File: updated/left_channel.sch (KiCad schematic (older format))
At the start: 24 parts, among them J2 Left 8 ohms, J3 Left 0 ohms, J7 Conn_Coaxial, T1 AudioTxfmr

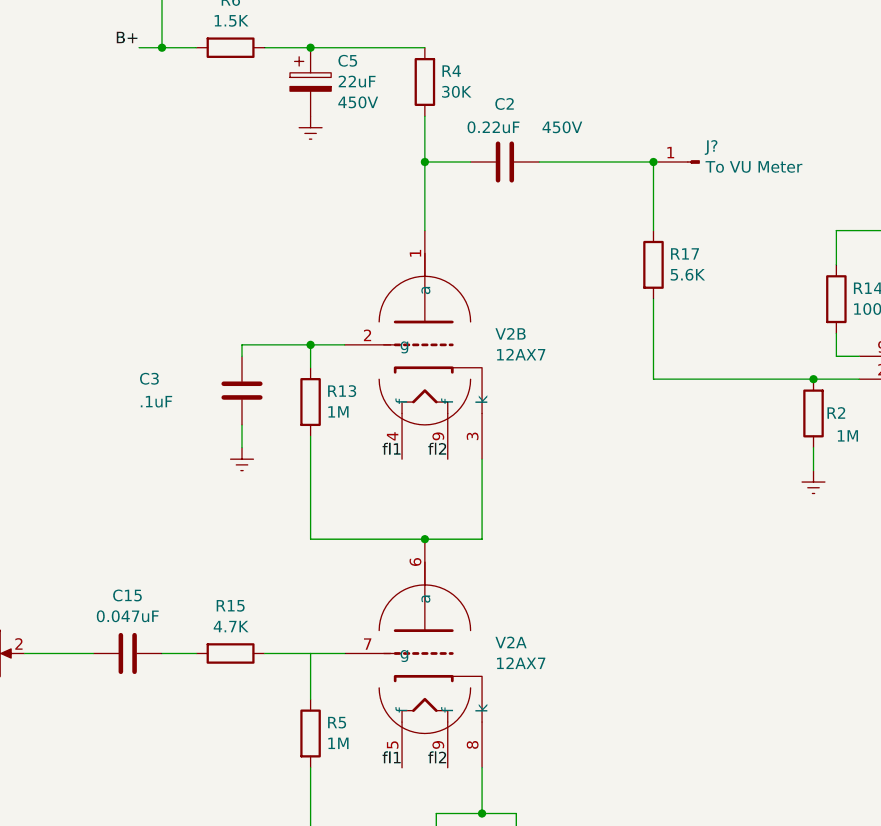
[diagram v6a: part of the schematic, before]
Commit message: remove grid stopped resistors.
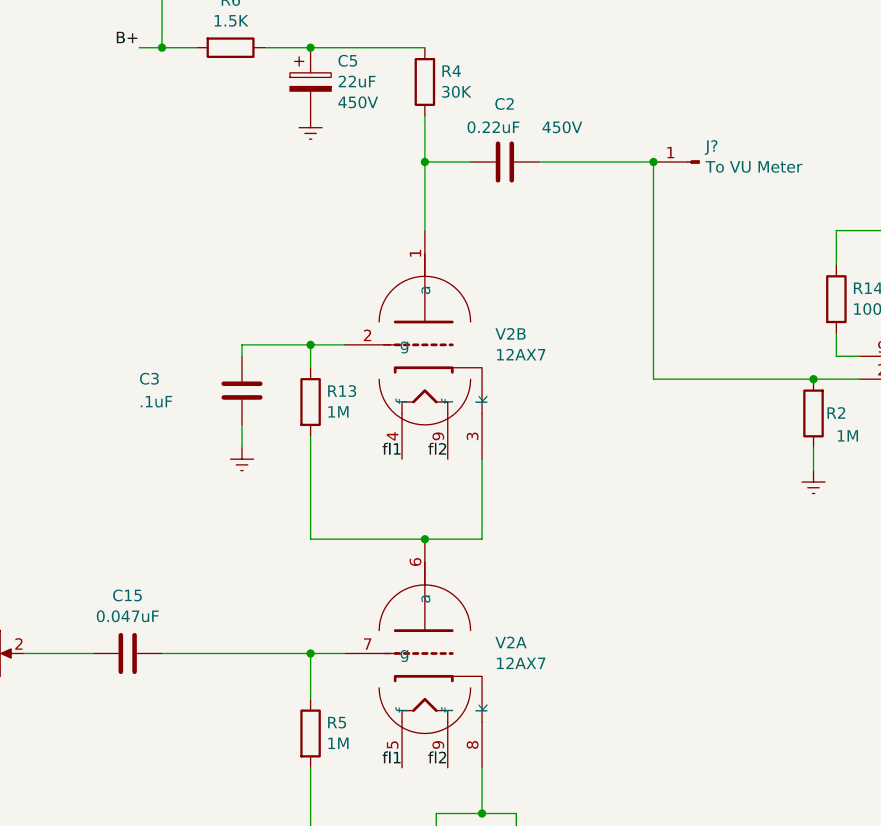
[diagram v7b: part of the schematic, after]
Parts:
- removed R15: 4.7K, symbol Device:R
- removed R17: 5.6K, symbol Device:R
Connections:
- net at R2.2, V3.2 (g1): now also C2.1, J?.1 (Pin_1)
- net at R5.1, V2.7 (g): now also C15.1
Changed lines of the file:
@@
 	0    1    1    0
 $EndComp
-$Comp
-L Device:R R?
-U 1 1 5F5B00DC
-P 3950 4500
-AR Path="/5F200EB9/5F5B00DC" Ref="R?"  Part="1"
-AR Path="/5F1F04D2/5F5B00DC" Ref="R15"  Part="1"
-F 0 "R15" V 3743 4500 50  0000 C CNN
-F 1 "4.7K" V 3834 4500 50  0000 C CNN
-F 2 "" V 3880 4500 50  0001 C CNN
-F 3 "~" H 3950 4500 50  0001 C CNN
-	1    3950 4500
-	0    1    1    0
-$EndComp
-Wire Wire Line
-	3650 4500 3800 4500
-Wire Wire Line
-	4100 4500 4300 4500
 Wire Wire Line
 	3050 4500 3350 4500
@@
 Connection ~ 4300 3150
 $Comp
-L Device:R R?
-U 1 1 5F5F04AC
-P 5800 2800
-AR Path="/5F200EB9/5F5F04AC" Ref="R?"  Part="1"
-AR Path="/5F1F04D2/5F5F04AC" Ref="R17"  Part="1"
-F 0 "R17" H 5870 2846 50  0000 L CNN
-F 1 "5.6K" H 5870 2755 50  0000 L CNN
-F 2 "" V 5730 2800 50  0001 C CNN
-F 3 "~" H 5800 2800 50  0001 C CNN
-	1    5800 2800
-	1    0    0    -1
-$EndComp
-Wire Wire Line
-	5800 2650 5800 2350
-Wire Wire Line
-	5800 2950 5800 3300
-$Comp
 L Connector:Conn_01x01_Male J?
 U 1 1 5F53BD18
@@
 $EndComp
 Connection ~ 5800 2350
+Wire Wire Line
+	5800 2350 5800 3300
+Connection ~ 4300 4500
+Wire Wire Line
+	3650 4500 4300 4500
 $EndSCHEMATC

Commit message: update schematic
Replaced all the counterfeit capacitor between preamp and power stage. Really opened up the sound.
Add some pictures
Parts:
- removed C2: 0.22uF, Capacitor_THT:CP_Radial_D4.0mm_P2.00mm, symbol Device:C
- added C? (x2): 0.1uF, symbol Device:C
- added J? (x2): Screw_Terminal_01x02, symbol Connector:Screw_Terminal_01x02
- added J? (x2): Conn_01x01_Male, symbol Connector:Conn_01x01_Male
- added Q? (x2): 2N4124, symbol Device:Q_NPN_EBC
- added R?: 100k, symbol Device:R
- added R?: 1, symbol Device:R
- added RV?: 100, symbol Device:R_Potentiometer
- C1, C4, C5: symbol Device:CP -> nobsound-audio-amplifier-rescue:CP-Device
- RV1: symbol Device:R_POT_Dual_Separate -> nobsound-audio-amplifier-rescue:R_POT_Dual_Separate-Device
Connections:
- net at J?.1 (Pin_1), R2.2, V3.2 (g1): now also C?.1, C?.1
- net at R4.1, V2.1 (a): now also C?.2, C?.2
- new net: J?.1 (Pin_1), J?.2 (Pin_2), Q?.1 (E), RV?.2
- new net: J?.1 (Pin_1), Q?.1 (E), Q?.2 (B), RV?.3
- new net: Q?.2 (B), Q?.3 (C), R?.2
- new net: J?.1 (Pin_1), Q?.3 (C), R?.1, R?.2
- new net: J?.1 (Pin_1), J?.2 (Pin_2), R?.1
- no-connect marks 1 -> 2
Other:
- note added: "362V"
- note added: "364V"
- note added: "I built this constant current source to experiment \nwith replacing the EL84 cathode lode resistor.\nIt worked. \nBut this design is only rated for 600mW. it gets warm just like the resistor.\nFor the complexity, this is not needed anyway."
- note added: "R = 2.2K\nV = 2.14V\nI=1.03mA"
- note added: "R = 30.7K\nV = 29.8V\nI = 0.98mA"
- note added: "R = 460\nV = 15.72V\nI = 34.2mA\nP = 538mW\n\nactual current: 68mA\n"
- note added: "V = 355V"
- note added: "V = 9\nI = 34.2mA\nP = 308mW"
- note added: "Vplate = 355 - 15.72\nVplate = 339.3V\nI = 34.2mA\nP = 11.6W\n\nactual:\n355-31.28=323.72\nP=22W"
- note added: "Vplate = 362 - 29.8 - 2.14\nVplate = \nI = 1.1mA\nP = 330mW"
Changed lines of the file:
@@
 	7050 2100 6900 2100
 $Comp
-L Device:CP C?
+L nobsound-audio-amplifier-rescue:CP-Device C?
 U 1 1 5F1FED3C
 P 4300 2000
@@
 $EndComp
 Connection ~ 4300 1850
-$Comp
-L Device:C C?
-U 1 1 5F1FED5C
-P 5150 2350
-AR Path="/5F1FED5C" Ref="C?"  Part="1"
-AR Path="/5F1F04D2/5F1FED5C" Ref="C2"  Part="1"
-F 0 "C2" V 4898 2350 50  0000 C CNN
-F 1 "0.22uF" V 5000 2300 50  0000 C CNN
-F 2 "Capacitor_THT:CP_Radial_D4.0mm_P2.00mm" H 5188 2200 50  0001 C CNN
-F 3 "~" H 5150 2350 50  0001 C CNN
-F 4 "450V" V 5000 2600 50  0000 C CNN "Voltage"
-	1    5150 2350
-	0    1    1    0
-$EndComp
 Wire Wire Line
 	5000 2350 4800 2350
@@
 $EndComp
 $Comp
-L Device:CP C?
+L nobsound-audio-amplifier-rescue:CP-Device C?
 U 1 1 5F1FEDAC
 P 5200 5500
@@
 	7050 2300 7050 2650
 $Comp
-L Device:CP C?
+L nobsound-audio-amplifier-rescue:CP-Device C?
 U 1 1 5F1FEDF9
 P 7450 4100
@@
 	7300 3650 7300 3850
 Wire Wire Line
-	7300 3850 7100 3850
-Wire Wire Line
-	7100 3850 7100 3950
-Wire Wire Line
 	7300 3850 7450 3850
 Wire Wire Line
 	7450 3850 7450 3950
-Connection ~ 7300 3850
-Wire Wire Line
-	7100 4250 7100 5900
-Wire Wire Line
-	7100 5900 5200 5900
 Connection ~ 5200 5900
 Wire Wire Line
 	7450 4250 7450 5900
-Wire Wire Line
-	7450 5900 7100 5900
-Connection ~ 7100 5900
 Wire Wire Line
 	3650 1850 3650 1600
@@
 	4800 4000 5050 4000
 $Comp
-L Device:R_POT_Dual_Separate RV1
+L nobsound-audio-amplifier-rescue:R_POT_Dual_Separate-Device RV1
 U 1 1 5F23DDB3
 P 2900 4500
@@
 Wire Wire Line
 	3650 4500 4300 4500
+Text Notes 3250 1750 0    50   ~ 0
+364V
+Text Notes 4650 1800 0    50   ~ 0
+362V
+Text Notes 4300 2650 0    50   ~ 0
+R = 30.7K\nV = 29.8V\nI = 0.98mA
+Text Notes 4400 5650 0    50   ~ 0
+R = 2.2K\nV = 2.14V\nI=1.03mA
+Text Notes 2750 3100 0    50   ~ 0
+Vplate = 362 - 29.8 - 2.14\nVplate = \nI = 1.1mA\nP = 330mW
+Text Notes 7150 2700 0    50   ~ 0
+V = 355V
+Text Notes 7900 4000 0    50   ~ 0
+R = 460\nV = 15.72V\nI = 34.2mA\nP = 538mW\n\nactual current: 68mA\n
+Text Notes 7700 3250 0    50   ~ 0
+Vplate = 355 - 15.72\nVplate = 339.3V\nI = 34.2mA\nP = 11.6W\n\nactual:\n355-31.28=323.72\nP=22W
+Text Notes 7500 1700 0    50   ~ 0
+V = 9\nI = 34.2mA\nP = 308mW
+$Comp
+L Device:Q_NPN_EBC Q?
+U 1 1 5F80FC62
+P 13400 4950
+F 0 "Q?" H 13591 4996 50  0000 L CNN
+F 1 "2N4124" H 13591 4905 50  0000 L CNN
+F 2 "" H 13600 5050 50  0001 C CNN
+F 3 "~" H 13400 4950 50  0001 C CNN
+	1    13400 4950
+	-1   0    0    -1
+$EndComp
+$Comp
+L Device:Q_NPN_EBC Q?
+U 1 1 5F8125CE
+P 13500 4600
+F 0 "Q?" H 13690 4646 50  0000 L CNN
+F 1 "2N4124" H 13690 4555 50  0000 L CNN
+F 2 "" H 13700 4700 50  0001 C CNN
+F 3 "~" H 13500 4600 50  0001 C CNN
+	1    13500 4600
+	1    0    0    -1
+$EndComp
+$Comp
+L Device:R R?
+U 1 1 5F81FC40
+P 13300 4300
+F 0 "R?" H 13370 4346 50  0000 L CNN
+F 1 "100k" H 13370 4255 50  0000 L CNN
+F 2 "" V 13230 4300 50  0001 C CNN
+F 3 "~" H 13300 4300 50  0001 C CNN
+	1    13300 4300
+	1    0    0    -1
+$EndComp
+$Comp
+L Device:R_Potentiometer RV?
+U 1 1 5F823B94
+P 13600 5250
+F 0 "RV?" H 13531 5204 50  0000 R CNN
+F 1 "100" H 13531 5295 50  0000 R CNN
+F 2 "" H 13600 5250 50  0001 C CNN
+F 3 "~" H 13600 5250 50  0001 C CNN
+	1    13600 5250
+	1    0    0    1
+$EndComp
+Wire Wire Line
+	13600 5100 13600 5050
+Wire Wire Line
+	13600 4800 13600 4950
+Connection ~ 13600 4950
+Wire Wire Line
+	13300 4600 13300 4750
+Wire Wire Line
+	13300 4600 13300 4450
+Connection ~ 13300 4600
+Wire Wire Line
+	13300 5150 13300 5400
+Wire Wire Line
+	13300 5400 13450 5400
+Wire Wire Line
+	13600 4400 13600 4150
+Wire Wire Line
+	13450 5400 13450 5500
+$Comp
+L Device:C C?
+U 1 1 5F848CBC
+P 5150 2250
+F 0 "C?" V 4898 2250 50  0000 C CNN
+F 1 "0.1uF" V 4989 2250 50  0000 C CNN
+F 2 "" H 5188 2100 50  0001 C CNN
+F 3 "~" H 5150 2250 50  0001 C CNN
+	1    5150 2250
+	0    1    1    0
+$EndComp
+$Comp
+L Device:C C?
+U 1 1 5F84A01F
+P 5150 2450
+F 0 "C?" V 5300 2350 50  0000 C CNN
+F 1 "0.1uF" V 5400 2350 50  0000 C CNN
+F 2 "" H 5188 2300 50  0001 C CNN
+F 3 "~" H 5150 2450 50  0001 C CNN
+	1    5150 2450
+	0    1    1    0
+$EndComp
+Wire Wire Line
+	5300 2250 5300 2350
+Wire Wire Line
+	5300 2350 5300 2450
+Connection ~ 5300 2350
+Wire Wire Line
+	5000 2250 5000 2350
+Wire Wire Line
+	5000 2350 5000 2450
+Connection ~ 5000 2350
+Wire Wire Line
+	13300 4150 13450 4150
+$Comp
+L Device:R R?
+U 1 1 5F85F894
+P 13450 4000
+F 0 "R?" H 13520 4046 50  0000 L CNN
+F 1 "1" H 13520 3955 50  0000 L CNN
+F 2 "" V 13380 4000 50  0001 C CNN
+F 3 "~" H 13450 4000 50  0001 C CNN
+	1    13450 4000
+	1    0    0    -1
+$EndComp
+Connection ~ 13450 4150
+Wire Wire Line
+	13450 4150 13600 4150
+$Comp
+L Connector:Screw_Terminal_01x02 J?
+U 1 1 5F860616
+P 12800 4700
+F 0 "J?" H 12718 4375 50  0000 C CNN
+F 1 "Screw_Terminal_01x02" H 12718 4466 50  0000 C CNN
+F 2 "" H 12800 4700 50  0001 C CNN
+F 3 "~" H 12800 4700 50  0001 C CNN
+	1    12800 4700
+	-1   0    0    1
+$EndComp
+Wire Wire Line
+	13000 4600 13000 3850
+Wire Wire Line
+	13000 3850 13450 3850
+Wire Wire Line
+	13000 4700 13000 5400
+Wire Wire Line
+	13000 5400 13300 5400
+Connection ~ 13300 5400
+Wire Wire Line
+	13450 3650 13450 3850
+Connection ~ 13450 3850
+$Comp
+L Connector:Conn_01x01_Male J?
+U 1 1 5F86F9E5
+P 13800 3850
+F 0 "J?" H 13772 3782 50  0000 R CNN
+F 1 "Conn_01x01_Male" H 13772 3873 50  0000 R CNN
+F 2 "" H 13800 3850 50  0001 C CNN
+F 3 "~" H 13800 3850 50  0001 C CNN
+	1    13800 3850
+	-1   0    0    1
+$EndComp
+$Comp
+L Connector:Conn_01x01_Male J?
+U 1 1 5F871049
+P 13800 4150
+F 0 "J?" H 13772 4082 50  0000 R CNN
+F 1 "Conn_01x01_Male" H 13772 4173 50  0000 R CNN
+F 2 "" H 13800 4150 50  0001 C CNN
+F 3 "~" H 13800 4150 50  0001 C CNN
+	1    13800 4150
+	-1   0    0    1
+$EndComp
+Connection ~ 13600 4150
+Wire Wire Line
+	13600 3850 13450 3850
+$Comp
+L Connector:Screw_Terminal_01x02 J?
+U 1 1 5F88DD97
+P 14100 5150
+F 0 "J?" H 14180 5142 50  0000 L CNN
+F 1 "Screw_Terminal_01x02" H 14180 5051 50  0000 L CNN
+F 2 "" H 14100 5150 50  0001 C CNN
+F 3 "~" H 14100 5150 50  0001 C CNN
+	1    14100 5150
+	1    0    0    -1
+$EndComp
+Wire Wire Line
+	13900 5150 13800 5150
+Wire Wire Line
+	13800 5150 13800 5050
+Wire Wire Line
+	13800 5050 13600 5050
+Connection ~ 13600 5050
+Wire Wire Line
+	13600 5050 13600 4950
+Wire Wire Line
+	13900 5250 13800 5250
+Wire Wire Line
+	13800 5250 13800 5500
+Wire Wire Line
+	13800 5500 13450 5500
+Connection ~ 13800 5250
+Wire Wire Line
+	13800 5250 13750 5250
+Connection ~ 13450 5500
+Wire Wire Line
+	13450 5500 13450 5700
+NoConn ~ 13600 5400
+Wire Wire Line
+	5200 5900 7100 5900
+Wire Wire Line
+	7300 3850 7100 3850
+Wire Wire Line
+	7100 3850 7100 3950
+Connection ~ 7300 3850
+Wire Wire Line
+	7100 4250 7100 5900
+Connection ~ 7100 5900
+Wire Wire Line
+	7100 5900 7450 5900
+Wire Notes Line
+	15650 3650 15650 6000
+Wire Notes Line
+	15650 6000 12150 6000
+Wire Notes Line
+	12150 3650 15650 3650
+Wire Notes Line
+	12150 3650 12150 6000
+Text Notes 12200 3600 0    50   ~ 0
+I built this constant current source to experiment \nwith replacing the EL84 cathode lode resistor.\nIt worked. \nBut this design is only rated for 600mW. it gets warm just like the resistor.\nFor the complexity, this is not needed anyway.
 $EndSCHEMATC
